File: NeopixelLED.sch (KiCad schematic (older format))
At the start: 2 parts

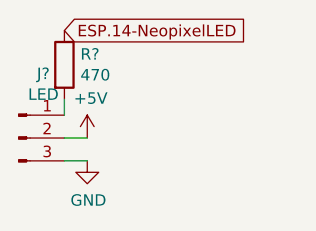
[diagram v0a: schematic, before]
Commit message: added sensors, finished schematics yet
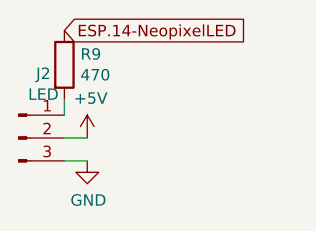
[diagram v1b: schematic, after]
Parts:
- J2: renamed from J?; footprint (none) -> TerminalBlock:ScrewTerminal_1x3_P5.00
- R9: renamed from R?; footprint (none) -> Resistor_THT:R_Axial_DIN0207_L6.3mm_D2.5mm_P7.62mm_Horizontal
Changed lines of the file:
@@
 $Descr A4 11693 8268
 encoding utf-8
-Sheet 11 13
+Sheet 11 14
 Title ""
 Date ""
@@
 $EndDescr
 $Comp
-L Connector:Conn_01x03_Male J?
+L Connector:Conn_01x03_Male J2
 U 1 1 60D34217
 P 5450 3460
-F 0 "J?" H 5558 3741 50  0000 C CNN
+F 0 "J2" H 5558 3741 50  0000 C CNN
 F 1 "LED" H 5558 3650 50  0000 C CNN
-F 2 "" H 5450 3460 50  0001 C CNN
+F 2 "TerminalBlock:ScrewTerminal_1x3_P5.00" H 5450 3460 50  0001 C CNN
 F 3 "~" H 5450 3460 50  0001 C CNN
 	1    5450 3460
@@
 $EndComp
 $Comp
-L power:GND #PWR?
+L power:GND #PWR0124
 U 1 1 60D346DF
 P 5750 3560
-F 0 "#PWR?" H 5750 3310 50  0001 C CNN
+F 0 "#PWR0124" H 5750 3310 50  0001 C CNN
 F 1 "GND" H 5755 3387 50  0000 C CNN
 F 2 "" H 5750 3560 50  0001 C CNN
@@
 $EndComp
 $Comp
-L power:+5V #PWR?
+L power:+5V #PWR0125
 U 1 1 60D35040
 P 5750 3460
-F 0 "#PWR?" H 5750 3310 50  0001 C CNN
+F 0 "#PWR0125" H 5750 3310 50  0001 C CNN
 F 1 "+5V" H 5765 3633 50  0000 C CNN
 F 2 "" H 5750 3460 50  0001 C CNN
@@
 	5650 3560 5750 3560
 $Comp
-L Device:R R?
+L Device:R R9
 U 1 1 60D35840
 P 5650 3140
-F 0 "R?" H 5720 3186 50  0000 L CNN
+F 0 "R9" H 5720 3186 50  0000 L CNN
 F 1 "470" H 5720 3095 50  0000 L CNN
-F 2 "" V 5580 3140 50  0001 C CNN
+F 2 "Resistor_THT:R_Axial_DIN0207_L6.3mm_D2.5mm_P7.62mm_Horizontal" V 5580 3140 50  0001 C CNN
 F 3 "~" H 5650 3140 50  0001 C CNN
 	1    5650 3140
